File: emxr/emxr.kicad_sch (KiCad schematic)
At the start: 10 parts, among them J101 POWER, J102 DSP_PW, J103 Bus Conn, J104 GEQ_L, J105 GEQ_L, J106 GEQ_R, J107 GEQ_R, J108 AUDIO_OUT

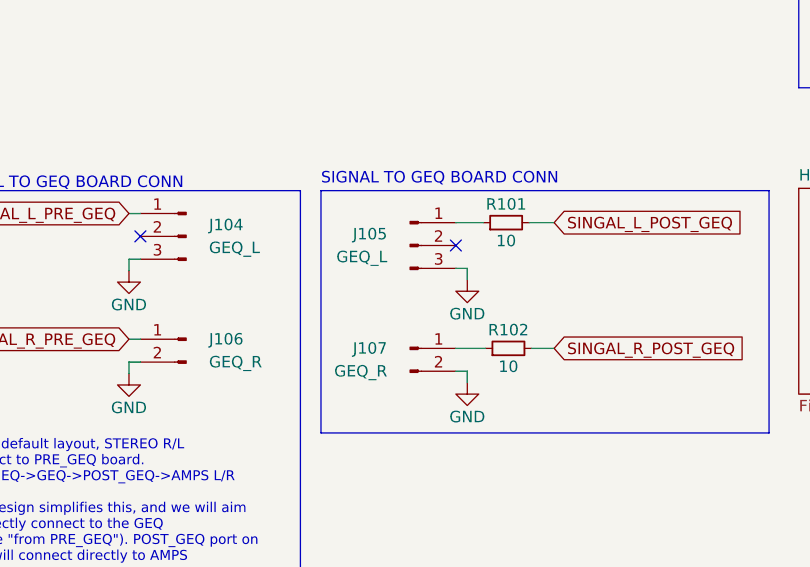
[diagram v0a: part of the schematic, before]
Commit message: finish footprints, starting on component placement
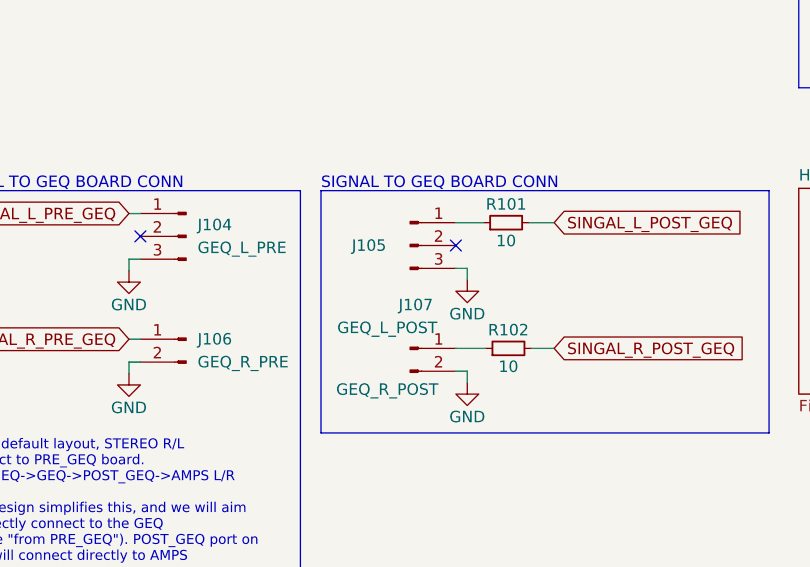
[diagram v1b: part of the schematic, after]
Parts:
- J101, J108: footprint (none) -> Connector_JST:JST_XH_B4B-XH-A_1x04_P2.50mm_Vertical
- J102: footprint (none) -> Connector_JST:JST_XH_B5B-XH-A_1x05_P2.50mm_Vertical
- J103: footprint (none) -> Connector_PinHeader_2.54mm:PinHeader_1x12_P2.54mm_Vertical
- J104: value GEQ_L -> GEQ_L_PRE; footprint (none) -> Connector_JST:JST_XH_B3B-XH-A_1x03_P2.50mm_Vertical
- J105: value GEQ_L -> GEQ_L_POST; footprint (none) -> Connector_JST:JST_XH_B3B-XH-A_1x03_P2.50mm_Vertical
- J106: value GEQ_R -> GEQ_R_PRE; footprint (none) -> Connector_JST:JST_XH_B2B-XH-A_1x02_P2.50mm_Vertical
- J107: value GEQ_R -> GEQ_R_POST; footprint (none) -> Connector_JST:JST_XH_B2B-XH-A_1x02_P2.50mm_Vertical
- R101, R102: footprint (none) -> Resistor_THT:R_Axial_DIN0207_L6.3mm_D2.5mm_P10.16mm_Horizontal

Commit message: replicated layout
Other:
- sheet Stereo renamed Stereo Channel L
- added sheet Stereo Channel R (stereo.kicad_sch)
- sheet Stereo Channel L ports: added SIGNAL_IN, SIGNAL_OUT; removed none

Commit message: more routing and reshuffling
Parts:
- removed J102: DSP_PW, Connector_JST:JST_XH_B5B-XH-A_1x05_P2.50mm_Vertical, symbol Connector:Conn_01x05_Male
- removed J103: Bus Conn, Connector_PinHeader_2.54mm:PinHeader_1x12_P2.54mm_Vertical, symbol Connector:Conn_01x12_Male
- added J103: Bus Conn, Connector_JST:JST_XH_B6B-XH-A_1x06_P2.50mm_Vertical, symbol Connector:Conn_01x06_Male
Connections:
- net +15V: now also J103.3 (Pin_3)
- net -15V: now also J103.2 (Pin_2)
- net BUS_L: now also J103.5 (Pin_5)
- net BUS_R: now also J103.4 (Pin_4)
- net GND: now also J108.3 (Pin_3), J103.6 (Pin_6); no longer J108.4 (Pin_4)
- net PHANTOM_PW: now also J103.1 (Pin_1)
- net SINGAL_L_POST_GEQ: now also J108.4 (Pin_4); no longer J108.1 (Pin_1)
- net SINGAL_R_POST_GEQ: now also J108.1 (Pin_1); no longer J108.3 (Pin_3)
- no-connect marks 5 -> 2
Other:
- note removed: "DSP Power Conn"
- note removed: "Do not connect?"
- moved on the sheet: J108

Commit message: first pcb draft
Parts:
- added H101, H102, H103, H104: MH, MountingHole:MountingHole_3.2mm_M3_DIN965_Pad_TopBottom, symbol Mechanical:MountingHole_Pad
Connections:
- net GND: now also J104.1 (Pin_1), H101.1, H102.1, H103.1, H104.1; no longer J104.3 (Pin_3)
- net SINGAL_L_PRE_GEQ: now also J104.3 (Pin_3); no longer J104.1 (Pin_1)
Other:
- moved on the sheet: J104

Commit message: finished pcb draft
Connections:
- net +15V: now also J103.2 (Pin_2); no longer J103.3 (Pin_3)
- net -15V: now also J103.3 (Pin_3); no longer J103.2 (Pin_2)
- net BUS_L: now also J103.4 (Pin_4); no longer J103.5 (Pin_5)
- net BUS_R: now also J103.5 (Pin_5); no longer J103.4 (Pin_4)
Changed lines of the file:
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@@
+    )
+  )
+  (global_label "BUS_L" (shape input) (at 72.898 37.084 0) (fields_autoplaced)
+    (effects (font (size 1.27 1.27)) (justify left))
+    (property "Intersheet References" "${INTERSHEET_REFS}" (id 0) (at 81.1168 37.0046 0)
+      (effects (font (size 1.27 1.27)) (justify left) hide)
     )
   )
@@
     )
   )
-  (global_label "BUS_L" (shape input) (at 72.898 39.624 0) (fields_autoplaced)
-    (effects (font (size 1.27 1.27)) (justify left))
-    (property "Intersheet References" "${INTERSHEET_REFS}" (id 0) (at 81.1168 39.5446 0)
-      (effects (font (size 1.27 1.27)) (justify left) hide)
-    )
-  )
   (global_label "SINGAL_L_POST_GEQ" (shape input) (at 254.254 103.886 180) (fields_autoplaced)
     (effects (font (size 1.27 1.27)) (justify right))
@@
     )
   )
-  (global_label "BUS_R" (shape input) (at 72.898 37.084 0) (fields_autoplaced)
-    (effects (font (size 1.27 1.27)) (justify left))
-    (property "Intersheet References" "${INTERSHEET_REFS}" (id 0) (at 81.3587 37.0046 0)
-      (effects (font (size 1.27 1.27)) (justify left) hide)
-    )
-  )
   (global_label "SINGAL_R_PRE_GEQ" (shape input) (at 115.57 110.49 180) (fields_autoplaced)
     (effects (font (size 1.27 1.27)) (justify right))
@@
     )
   )
+  (global_label "BUS_R" (shape input) (at 72.898 39.624 0) (fields_autoplaced)
+    (effects (font (size 1.27 1.27)) (justify left))
+    (property "Intersheet References" "${INTERSHEET_REFS}" (id 0) (at 81.3587 39.5446 0)
+      (effects (font (size 1.27 1.27)) (justify left) hide)
+    )
+  )
   (symbol (lib_id "Connector:Conn_01x04_Male") (at 21.336 29.972 0) (unit 1)
     (in_bom yes) (on_board yes) (fields_autoplaced)
@@
     (pin "4")
   )
+  (symbol (lib_id "power:-15V") (at 97.282 29.972 0) (unit 1)
+    (in_bom yes) (on_board yes) (fields_autoplaced)
+    (property "Reference" "#PWR0117" (id 0) (at 97.282 27.432 0)
+      (effects (font (size 1.27 1.27)) hide)
+    )
+    (property "Value" "-15V" (id 1) (at 97.282 24.892 0))
+    (property "Footprint" "" (id 2) (at 97.282 29.972 0)
+      (effects (font (size 1.27 1.27)) hide)
+    )
+    (property "Datasheet" "" (id 3) (at 97.282 29.972 0)
+      (effects (font (size 1.27 1.27)) hide)
+    )
+    (pin "1")
+  )
   (symbol (lib_id "Mechanical:MountingHole_Pad") (at 34.036 60.706 0) (unit 1)
     (in_bom yes) (on_board yes) (fields_autoplaced)
@@
     (pin "1")
     (pin "2")
-  )
-  (symbol (lib_id "power:-15V") (at 36.576 26.162 0) (unit 1)
-    (in_bom yes) (on_board yes) (fields_autoplaced)
-    (property "Reference" "#PWR0102" (id 0) (at 36.576 23.622 0)
-      (effects (font (size 1.27 1.27)) hide)
-    )
-    (property "Value" "-15V" (id 1) (at 36.576 21.082 0))
-    (property "Footprint" "" (id 2) (at 36.576 26.162 0)
-      (effects (font (size 1.27 1.27)) hide)
-    )
-    (property "Datasheet" "" (id 3) (at 36.576 26.162 0)
-      (effects (font (size 1.27 1.27)) hide)
-    )
-    (pin "1")
   )
   (symbol (lib_id "power:GND") (at 28.956 37.592 0) (unit 1)
@@
     (pin "2")
   )
+  (symbol (lib_id "power:-15V") (at 36.576 26.162 0) (unit 1)
+    (in_bom yes) (on_board yes) (fields_autoplaced)
+    (property "Reference" "#PWR0102" (id 0) (at 36.576 23.622 0)
+      (effects (font (size 1.27 1.27)) hide)
+    )
+    (property "Value" "-15V" (id 1) (at 36.576 21.082 0))
+    (property "Footprint" "" (id 2) (at 36.576 26.162 0)
+      (effects (font (size 1.27 1.27)) hide)
+    )
+    (property "Datasheet" "" (id 3) (at 36.576 26.162 0)
+      (effects (font (size 1.27 1.27)) hide)
+    )
+    (pin "1")
+  )
   (symbol (lib_id "power:GND") (at 115.57 102.87 0) (unit 1)
     (in_bom yes) (on_board yes)
@@
     (pin "1")
   )
-  (symbol (lib_id "power:-15V") (at 90.932 29.972 0) (unit 1)
-    (in_bom yes) (on_board yes) (fields_autoplaced)
-    (property "Reference" "#PWR0117" (id 0) (at 90.932 27.432 0)
-      (effects (font (size 1.27 1.27)) hide)
-    )
-    (property "Value" "-15V" (id 1) (at 90.932 24.892 0))
-    (property "Footprint" "" (id 2) (at 90.932 29.972 0)
-      (effects (font (size 1.27 1.27)) hide)
-    )
-    (property "Datasheet" "" (id 3) (at 90.932 29.972 0)
+  (symbol (lib_id "power:+15V") (at 30.226 26.162 0) (unit 1)
+    (in_bom yes) (on_board yes) (fields_autoplaced)
+    (property "Reference" "#PWR0101" (id 0) (at 30.226 29.972 0)
+      (effects (font (size 1.27 1.27)) hide)
+    )
+    (property "Value" "+15V" (id 1) (at 30.226 21.082 0))
+    (property "Footprint" "" (id 2) (at 30.226 26.162 0)
+      (effects (font (size 1.27 1.27)) hide)
+    )
+    (property "Datasheet" "" (id 3) (at 30.226 26.162 0)
       (effects (font (size 1.27 1.27)) hide)
     )
@@
     (pin "3")
   )
+  (symbol (lib_id "power:+15V") (at 90.932 29.972 0) (unit 1)
+    (in_bom yes) (on_board yes)
+    (property "Reference" "#PWR0105" (id 0) (at 90.932 33.782 0)
+      (effects (font (size 1.27 1.27)) hide)
+    )
+    (property "Value" "+15V" (id 1) (at 90.932 24.892 0))
+    (property "Footprint" "" (id 2) (at 90.932 29.972 0)
+      (effects (font (size 1.27 1.27)) hide)
+    )
+    (property "Datasheet" "" (id 3) (at 90.932 29.972 0)
+      (effects (font (size 1.27 1.27)) hide)
+    )
+    (pin "1")
+  )
   (symbol (lib_id "Mechanical:MountingHole_Pad") (at 18.542 60.706 0) (unit 1)
     (in_bom yes) (on_board yes) (fields_autoplaced)
@@
     )
     (property "Datasheet" "~" (id 3) (at 27.94 27.432 0)
-      (effects (font (size 1.27 1.27)) hide)
-    )
-    (pin "1")
-  )
-  (symbol (lib_id "power:+15V") (at 97.282 29.972 0) (unit 1)
-    (in_bom yes) (on_board yes)
-    (property "Reference" "#PWR0105" (id 0) (at 97.282 33.782 0)
-      (effects (font (size 1.27 1.27)) hide)
-    )
-    (property "Value" "+15V" (id 1) (at 97.282 24.892 0))
-    (property "Footprint" "" (id 2) (at 97.282 29.972 0)
-      (effects (font (size 1.27 1.27)) hide)
-    )
-    (property "Datasheet" "" (id 3) (at 97.282 29.972 0)
-      (effects (font (size 1.27 1.27)) hide)
-    )
-    (pin "1")
-  )
-  (symbol (lib_id "power:+15V") (at 30.226 26.162 0) (unit 1)
-    (in_bom yes) (on_board yes) (fields_autoplaced)
-    (property "Reference" "#PWR0101" (id 0) (at 30.226 29.972 0)
-      (effects (font (size 1.27 1.27)) hide)
-    )
-    (property "Value" "+15V" (id 1) (at 30.226 21.082 0))
-    (property "Footprint" "" (id 2) (at 30.226 26.162 0)
-      (effects (font (size 1.27 1.27)) hide)
-    )
-    (property "Datasheet" "" (id 3) (at 30.226 26.162 0)
       (effects (font (size 1.27 1.27)) hide)
     )
@@
       (reference "#FLG0302") (unit 1) (value "PWR_FLAG") (footprint "")
     )
-    (path "/f7fcb284-2c50-4899-a801-6bc09b570947"
+    (path "/ca94f7d8-1a2e-4977-bdda-6569c606eee3"
       (reference "#PWR0101") (unit 1) (value "+15V") (footprint "")
     )
-    (path "/318c314c-3085-4786-b774-c74338b7a2e5"
+    (path "/969dab04-7c43-4161-8376-eb4539bfe8f0"
       (reference "#PWR0102") (unit 1) (value "-15V") (footprint "")
     )
@@
       (reference "#PWR0104") (unit 1) (value "GND") (footprint "")
     )
-    (path "/ee4aa2f5-45df-4dae-abad-1cf46d567827"
+    (path "/daf14d0e-21df-46a4-877f-4f85481a5d4a"
       (reference "#PWR0105") (unit 1) (value "+15V") (footprint "")
     )
@@
       (reference "#PWR0116") (unit 1) (value "GND") (footprint "")
     )
-    (path "/d20691b9-17e8-4af0-b9bd-2f8e4c1bd205"
+    (path "/1290aab4-682e-4097-b981-7d63f0a8b5a2"
       (reference "#PWR0117") (unit 1) (value "-15V") (footprint "")
     )

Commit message: more cleaning up/finishing touches
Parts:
- removed J106: GEQ_R_PRE, Connector_JST:JST_XH_B2B-XH-A_1x02_P2.50mm_Vertical, symbol Connector:Conn_01x02_Male
- removed J107: GEQ_R_POST, Connector_JST:JST_XH_B2B-XH-A_1x02_P2.50mm_Vertical, symbol Connector:Conn_01x02_Male
- added H105, H106, H107: MH, MountingHole:MountingHole_3.2mm_M3_DIN965_Pad_TopBottom, symbol Mechanical:MountingHole_Pad
- J104: value GEQ_L_PRE -> GEQ_PRE
- J105: value GEQ_L_POST -> GEQ_POST
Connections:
- net GND: now also H105.1, H106.1, H107.1
- net SINGAL_R_PRE_GEQ: now also J104.2 (Pin_2)
- net at R101.1: now also J105.2 (Pin_2); no longer J105.1 (Pin_1)
- net at R102.1: now also J105.1 (Pin_1)
- no-connect marks 2 -> 0
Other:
- moved on the sheet: H101, H102, H103, H104, J104, J105, R101, R102
